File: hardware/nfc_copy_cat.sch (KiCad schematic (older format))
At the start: 35 parts, among them J1 USB_B_Micro, J2 Battery, J3 SWD, J4 NFC Module V3, J5 Conn_01x02, J6 Adafruit NFC 1.0, SW1 RST, SW2 Magspoof, SW3 NFC, U1 AP2112K-3.3TRG1, U2 MCP73831-2-OT, U3 TC4424, U4 ATSAMD21E18A, U5 GD25Q16C

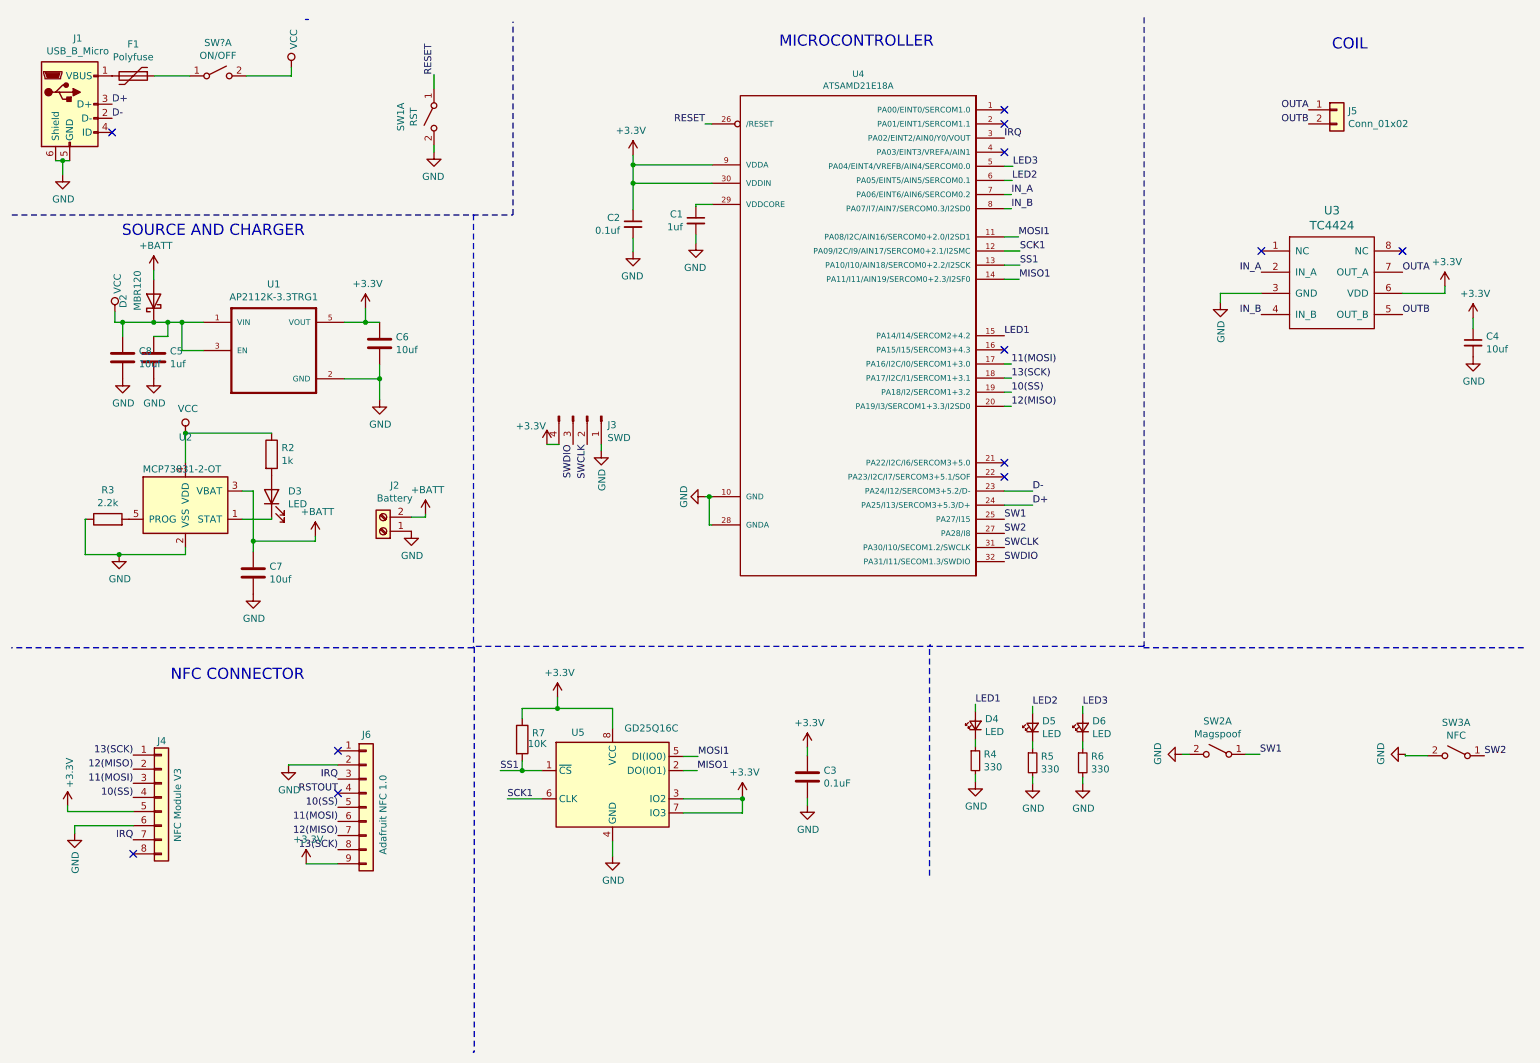
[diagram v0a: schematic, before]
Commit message: change battery source driver
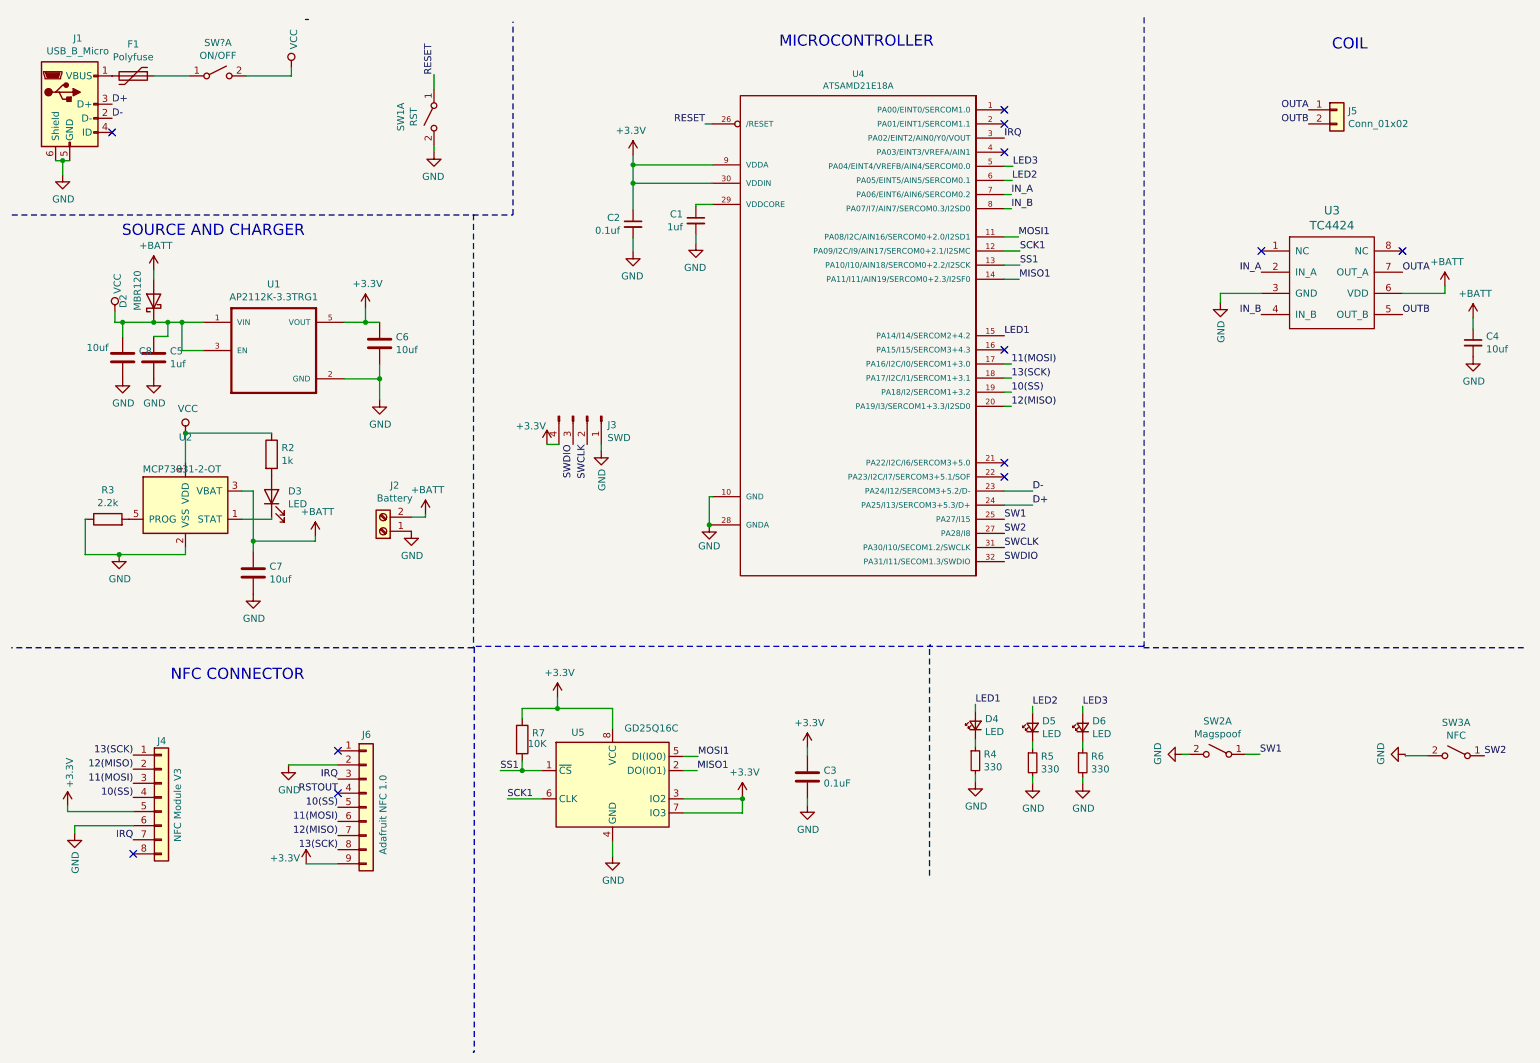
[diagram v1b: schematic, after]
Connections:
- net +3V3: no longer C4.1, U3.6 (VDD)
- net +BATT: now also C4.1, U3.6 (VDD)
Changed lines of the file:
@@
 L nfc_copy_cat-rescue:GND-MagSpoofTC-cache #PWR010
 U 1 1 5D10E10D
-P 5380 3860
-F 0 "#PWR010" H 5380 3610 50  0001 C CNN
-F 1 "GND" H 5380 3710 50  0000 C CNN
-F 2 "" H 5380 3860 50  0000 C CNN
-F 3 "" H 5380 3860 50  0000 C CNN
-	1    5380 3860
-	0    1    -1   0
-$EndComp
-Wire Wire Line
-	5380 3860 5410 3860
+P 5410 4060
+F 0 "#PWR010" H 5410 3810 50  0001 C CNN
+F 1 "GND" H 5410 3910 50  0000 C CNN
+F 2 "" H 5410 4060 50  0000 C CNN
+F 3 "" H 5410 4060 50  0000 C CNN
+	1    5410 4060
+	-1   0    0    -1
+$EndComp
 Text Label 5380 1220 2    50   ~ 0
 RESET
@@
 Wire Wire Line
 	5410 4060 5430 4060
-Connection ~ 5410 3860
 Wire Wire Line
 	5410 3860 5430 3860
@@
 P 1255 2875
 F 0 "C8" H 1370 2921 50  0000 L CNN
-F 1 "10uf" H 1370 2830 50  0000 L CNN
+F 1 "10uf" H 1000 2945 50  0000 L CNN
 F 2 "Capacitor_SMD:C_0805_2012Metric_Pad1.15x1.40mm_HandSolder" H 1293 2725 50  0001 C CNN
 F 3 "~" H 1255 2875 50  0001 C CNN
@@
 P 2555 6460
 F 0 "#PWR0101" H 2555 6310 50  0001 C CNN
-F 1 "+3.3V" H 2570 6633 50  0000 C CNN
+F 1 "+3.3V" H 2405 6500 50  0000 C CNN
 F 2 "" H 2555 6460 50  0001 C CNN
 F 3 "" H 2555 6460 50  0001 C CNN
@@
 	1700 3410 2310 3410
 NoConn ~ 2780 5960
-$Comp
-L power:+3.3V #PWR?
-U 1 1 5E3E4F66
-P 10820 2595
-F 0 "#PWR?" H 10820 2445 50  0001 C CNN
-F 1 "+3.3V" H 10835 2768 50  0000 C CNN
-F 2 "" H 10820 2595 50  0001 C CNN
-F 3 "" H 10820 2595 50  0001 C CNN
-	1    10820 2595
-	1    0    0    -1
-$EndComp
 Text Label 10320 2570 0    50   ~ 0
 OUTB
@@
 $EndComp
 $Comp
-L power:+3.3V #PWR019
-U 1 1 5D10F76C
-P 10620 2370
-F 0 "#PWR019" H 10620 2220 50  0001 C CNN
-F 1 "+3.3V" H 10635 2543 50  0000 C CNN
-F 2 "" H 10620 2370 50  0001 C CNN
-F 3 "" H 10620 2370 50  0001 C CNN
-	1    10620 2370
-	1    0    0    -1
-$EndComp
-$Comp
 L Device:C_Small C4
 U 1 1 5D11FCB0
@@
 	1255 2625 1200 2625
 Connection ~ 1700 3410
+Connection ~ 5410 4060
+$Comp
+L power:+BATT #PWR?
+U 1 1 6080D6FF
+P 10620 2370
+F 0 "#PWR?" H 10620 2220 50  0001 C CNN
+F 1 "+BATT" H 10635 2543 50  0000 C CNN
+F 2 "" H 10620 2370 50  0001 C CNN
+F 3 "" H 10620 2370 50  0001 C CNN
+	1    10620 2370
+	1    0    0    -1
+$EndComp
+$Comp
+L power:+BATT #PWR?
+U 1 1 6080F77B
+P 10820 2595
+F 0 "#PWR?" H 10820 2445 50  0001 C CNN
+F 1 "+BATT" H 10835 2768 50  0000 C CNN
+F 2 "" H 10820 2595 50  0001 C CNN
+F 3 "" H 10820 2595 50  0001 C CNN
+	1    10820 2595
+	1    0    0    -1
+$EndComp
 $EndSCHEMATC

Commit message: updateSchm
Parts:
- added C?: 1uf, Capacitor_SMD:C_0805_2012Metric_Pad1.15x1.40mm_HandSolder, symbol Device:C_Small
- added C?: 0.1uf, Capacitor_SMD:C_0805_2012Metric_Pad1.15x1.40mm_HandSolder, symbol Device:C_Small
- added U?: ATSAMD21E18A, Package_QFP:TQFP-32_7x7mm_P0.8mm, symbol nfc_copy_cat-rescue:ATSAMD21E18A-electroniccats
- U4: footprint Package_QFP:TQFP-32_7x7mm_P0.8mm -> Package_DFN_QFN:QFN-32-1EP_5x5mm_P0.5mm_EP3.6x3.6mm
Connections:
- net +3V3: now also C?.1, U?.30 (VDDIN), U?.9 (VDDA)
- net 10(SS): now also U?.19 (PA18/I2/SERCOM1+3.2)
- net 11(MOSI): now also U?.17 (PA16/I2C/I0/SERCOM1+3.0)
- net 12(MISO): now also U?.20 (PA19/I3/SERCOM1+3.3/I2SD0)
- net 13(SCK): now also U?.18 (PA17/I2C/I1/SERCOM1+3.1)
- net D+: now also U?.24 (PA25/I13/SERCOM3+5.3/D+)
- net D-: now also U?.23 (PA24/I12/SERCOM3+5.2/D-)
- net GND: now also C?.2, C?.2, U?.10 (GND), U?.28 (GNDA)
- net IN_A: now also U?.7 (PA06/EINT6/AIN6/SERCOM0.2)
- net IN_B: now also U?.8 (PA07/I7/AIN7/SERCOM0.3/I2SD0)
- net IRQ: now also U?.3 (PA02/EINT2/AIN0/Y0/VOUT)
- net LED1: now also U?.15 (PA14/I14/SERCOM2+4.2)
- net LED2: now also U?.6 (PA05/EINT5/AIN5/SERCOM0.1)
- net LED3: now also U?.5 (PA04/EINT4/VREFB/AIN4/SERCOM0.0)
- net MISO1: now also U?.14 (PA11/I11/AIN19/SERCOM0+2.3/I2SF0)
- net MOSI1: now also U?.11 (PA08/I2C/AIN16/SERCOM0+2.0/I2SD1)
- net RESET: now also U?.26 (/RESET)
- net SCK1: now also U?.12 (PA09/I2C/I9/AIN17/SERCOM0+2.1/I2SMC)
- net SS1: now also U?.13 (PA10/I10/AIN18/SERCOM0+2.2/I2SCK)
- net SW1: now also U?.25 (PA27/I15)
- net SW2: now also U?.27 (PA28/I8)
- net SWCLK: now also U?.31 (PA30/I10/SECOM1.2/SWCLK)
- net SWDIO: now also U?.32 (PA31/I11/SECOM1.3/SWDIO)
- new net: C?.1, U?.29 (VDDCORE)
- no-connect marks 12 -> 18
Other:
- note added: "BUTTONS"
- note added: "LEDS"
- note added: "QFN"
- note added: "SWD"
- note added: "TQFN"
- moved on the sheet: C1, C2, C3, C4, C5, C6, C7, C8, D2, D3, D4, D5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

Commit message: updatingPCB
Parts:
- removed C?: 1uf, Capacitor_SMD:C_0805_2012Metric_Pad1.15x1.40mm_HandSolder, symbol Device:C_Small
- removed C?: 0.1uf, Capacitor_SMD:C_0805_2012Metric_Pad1.15x1.40mm_HandSolder, symbol Device:C_Small
- gave numbers to parts that had none: 2
- renumbered C6 to C1, C8 to C3, C5 to C4, C1 to C5, C7 to C6, C3 to C7, C4 to C8, D2 to D1, D3 to D2, D4 to D3, D5 to D4, D6 to D5, J4 to J3, J6 to J4, J3 to J6, R2 to R1, R3 to R2, R7 to R3, SW1 to SW2, SW2 to SW3, SW3 to SW4, U4 to U2, U2 to U4, U3 to U5, U5 to U6
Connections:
- net VDDCORE: now reaches C5.1, U2.29 (VDDCORE)
- net VDDCORE: now also U3.29 (VDDCORE)
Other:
- moved on the sheet: C2, C5

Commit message: NRoutinginProgress
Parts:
- R1: footprint Resistor_SMD:R_0805_2012Metric_Pad1.15x1.40mm_HandSolder -> Resistor_SMD:R_0805_2012Metric
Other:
- moved on the sheet: F1
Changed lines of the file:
@@
 $EndDescr
-$Comp
-L nfc_copy_cat-rescue:USB_B_Micro-Connector J1
-U 1 1 5D106D67
-P 880 1080
-F 0 "J1" H 937 1547 50  0000 C CNN
-F 1 "USB_B_Micro" H 937 1456 50  0000 C CNN
-F 2 "Connectors:U254051N4BH806" H 1030 1030 50  0001 C CNN
-F 3 "~" H 1030 1030 50  0001 C CNN
-	1    880  1080
-	1    0    0    -1
-$EndComp
 $Comp
 L nfc_copy_cat-rescue:GND-MagSpoofTC-cache #PWR03
@@
 L Device:Polyfuse F1
 U 1 1 5D119569
-P 1330 880
-F 0 "F1" V 1105 880 50  0000 C CNN
-F 1 "Polyfuse" V 1196 880 50  0000 C CNN
-F 2 "Fuse:Fuse_0805_2012Metric_Pad1.15x1.40mm_HandSolder" H 1380 680 50  0001 L CNN
-F 3 "~" H 1330 880 50  0001 C CNN
-F 4 "MFU0805FF00500P100" V 1330 880 50  0001 C CNN "manf#"
-	1    1330 880
+P 1355 880
+F 0 "F1" V 1130 880 50  0000 C CNN
+F 1 "Polyfuse" V 1221 880 50  0000 C CNN
+F 2 "Fuse:Fuse_0805_2012Metric_Pad1.15x1.40mm_HandSolder" H 1405 680 50  0001 L CNN
+F 3 "~" H 1355 880 50  0001 C CNN
+F 4 "MFU0805FF00500P100" V 1355 880 50  0001 C CNN "manf#"
+	1    1355 880
 	0    1    1    0
 $EndComp
@@
 F 0 "R1" H 1960 3641 50  0000 L CNN
 F 1 "1k" H 1960 3550 50  0000 L CNN
-F 2 "Resistor_SMD:R_0805_2012Metric_Pad1.15x1.40mm_HandSolder" V 1820 3595 50  0001 C CNN
+F 2 "Resistor_SMD:R_0805_2012Metric" V 1820 3595 50  0001 C CNN
 F 3 "~" H 1890 3595 50  0001 C CNN
 	1    1890 3595
@@
 	1    0    0    -1
 $EndComp
-Wire Wire Line
-	1480 880  1730 880
 Wire Wire Line
 	2130 880  2450 880
@@
 Wire Wire Line
 	7940 1660 8045 1660
+$Comp
+L nfc_copy_cat-rescue:USB_B_Micro-Connector J1
+U 1 1 5D106D67
+P 880 1080
+F 0 "J1" H 937 1547 50  0000 C CNN
+F 1 "USB_B_Micro" H 937 1456 50  0000 C CNN
+F 2 "Connectors:U254051N4BH806" H 1030 1030 50  0001 C CNN
+F 3 "~" H 1030 1030 50  0001 C CNN
+	1    880  1080
+	1    0    0    -1
+$EndComp
+Wire Wire Line
+	1180 880  1205 880
+Wire Wire Line
+	1505 880  1730 880
 $EndSCHEMATC

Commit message: fixButtonSchm
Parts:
- removed SW2: RST, Button_Switch_SMD:SW_SPST_TL3342, symbol nfc_copy_cat-rescue:SW_DPST_x2-Switch
- removed SW3: Magspoof, Button_Switch_SMD:SW_SPST_TL3342, symbol nfc_copy_cat-rescue:SW_DPST_x2-Switch
- removed SW4: NFC, Button_Switch_SMD:SW_SPST_TL3342, symbol nfc_copy_cat-rescue:SW_DPST_x2-Switch
- added SW2: RST, Button_Switch_SMD:SW_SPST_TL3342, symbol Bast_WAN-cache:Switch_SW_Push
- added SW3: Magspoof, Button_Switch_SMD:SW_SPST_TL3342, symbol Bast_WAN-cache:Switch_SW_Push
- added SW4: NFC, Button_Switch_SMD:SW_SPST_TL3342, symbol Bast_WAN-cache:Switch_SW_Push
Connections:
- net GND: now also SW2.1, SW3.1, SW4.1
- net RESET: now also SW2.2
- net SW1: now also SW3.2
- net SW2: now also SW4.2
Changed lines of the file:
@@
 	-1   0    0    -1
 $EndComp
-Wire Wire Line
-	2955 1380 2955 1430
 $Comp
 L nfc_copy_cat-rescue:GND-MagSpoofTC-cache #PWR02
 U 1 1 5D116DE8
-P 2955 1430
-F 0 "#PWR02" H 2955 1180 50  0001 C CNN
-F 1 "GND" H 2960 1257 50  0000 C CNN
-F 2 "" H 2955 1430 50  0000 C CNN
-F 3 "" H 2955 1430 50  0000 C CNN
-	1    2955 1430
+P 600 7050
+F 0 "#PWR02" H 600 6800 50  0001 C CNN
+F 1 "GND" H 605 6877 50  0000 C CNN
+F 2 "" H 600 7050 50  0000 C CNN
+F 3 "" H 600 7050 50  0000 C CNN
+	1    600  7050
 	-1   0    0    -1
 $EndComp
-Wire Wire Line
-	2955 880  2955 980
-Text Label 2955 880  1    50   ~ 0
+Text Label 1150 7000 0    50   ~ 0
 RESET
-$Comp
-L nfc_copy_cat-rescue:SW_DPST_x2-Switch SW2
-U 1 1 5D1166AC
-P 2955 1180
-F 0 "SW2" H 2955 1415 50  0000 C CNN
-F 1 "RST" H 2955 1324 50  0000 C CNN
-F 2 "Button_Switch_SMD:SW_SPST_TL3342" H 2955 1180 50  0001 C CNN
-F 3 "~" H 2955 1180 50  0001 C CNN
-	1    2955 1180
-	0    -1   1    0
-$EndComp
 Wire Wire Line
 	4170 4010 4170 4210
@@
 Text Label 6260 4270 0    50   ~ 0
 SW2
-Wire Wire Line
-	965  7415 915  7415
 $Comp
 L nfc_copy_cat-rescue:GND-MagSpoofTC-cache #PWR039
 U 1 1 5D38B380
-P 915 7415
-F 0 "#PWR039" H 915 7165 50  0001 C CNN
-F 1 "GND" H 920 7242 50  0000 C CNN
-F 2 "" H 915 7415 50  0000 C CNN
-F 3 "" H 915 7415 50  0000 C CNN
-	1    915  7415
-	0    1    -1   0
-$EndComp
-Text Label 1465 7415 0    50   ~ 0
+P 1545 7080
+F 0 "#PWR039" H 1545 6830 50  0001 C CNN
+F 1 "GND" H 1550 6907 50  0000 C CNN
+F 2 "" H 1545 7080 50  0000 C CNN
+F 3 "" H 1545 7080 50  0000 C CNN
+	1    1545 7080
+	-1   0    0    -1
+$EndComp
+Text Label 2035 7000 0    50   ~ 0
 SW1
-$Comp
-L nfc_copy_cat-rescue:SW_DPST_x2-Switch SW3
-U 1 1 5D38B388
-P 1165 7415
-F 0 "SW3" H 1165 7650 50  0000 C CNN
-F 1 "Magspoof" H 1165 7559 50  0000 C CNN
-F 2 "Button_Switch_SMD:SW_SPST_TL3342" H 1165 7415 50  0001 C CNN
-F 3 "~" H 1165 7415 50  0001 C CNN
-	1    1165 7415
-	-1   0    0    -1
-$EndComp
-$Comp
-L nfc_copy_cat-rescue:SW_DPST_x2-Switch SW4
-U 1 1 5D3AF4BF
-P 2855 7425
-F 0 "SW4" H 2855 7660 50  0000 C CNN
-F 1 "NFC" H 2855 7569 50  0000 C CNN
-F 2 "Button_Switch_SMD:SW_SPST_TL3342" H 2855 7425 50  0001 C CNN
-F 3 "~" H 2855 7425 50  0001 C CNN
-	1    2855 7425
-	-1   0    0    -1
-$EndComp
 $Comp
 L nfc_copy_cat-rescue:GND-MagSpoofTC-cache #PWR040
 U 1 1 5D3B020B
-P 2495 7415
-F 0 "#PWR040" H 2495 7165 50  0001 C CNN
-F 1 "GND" H 2500 7242 50  0000 C CNN
-F 2 "" H 2495 7415 50  0000 C CNN
-F 3 "" H 2495 7415 50  0000 C CNN
-	1    2495 7415
-	0    1    -1   0
-$EndComp
-Wire Wire Line
-	2655 7425 2495 7425
-Wire Wire Line
-	2495 7425 2495 7415
-Text Label 3055 7425 0    50   ~ 0
+P 2430 7060
+F 0 "#PWR040" H 2430 6810 50  0001 C CNN
+F 1 "GND" H 2435 6887 50  0000 C CNN
+F 2 "" H 2430 7060 50  0000 C CNN
+F 3 "" H 2430 7060 50  0000 C CNN
+	1    2430 7060
+	-1   0    0    -1
+$EndComp
+Text Label 2920 7010 0    50   ~ 0
 SW2
 Text Label 6260 1470 0    50   ~ 0
 IRQ
-Wire Wire Line
-	1365 7415 1465 7415
 $Comp
 L Device:LED_Small D3
@@
 Wire Wire Line
 	7220 5830 7220 5895
-$Comp
-L nfc_copy_cat-rescue:SW_DPST_x2-Switch SW1
-U 1 1 607BCC65
-P 1930 880
-F 0 "SW1" H 1930 1115 50  0000 C CNN
-F 1 "ON/OFF" H 1930 1024 50  0000 C CNN
-F 2 "" H 1930 880 50  0001 C CNN
-F 3 "" H 1930 880 50  0001 C CNN
-	1    1930 880
-	1    0    0    -1
-$EndComp
 Wire Wire Line
 	2130 880  2450 880
@@
 Wire Notes Line
 	6965 6630 6965 6380
-Text Notes 1385 6760 0    79   ~ 0
+Text Notes 1100 6620 0    79   ~ 0
 BUTTONS
 Wire Notes Line
@@
 Wire Wire Line
 	1505 880  1730 880
+$Comp
+L nfc_copy_cat-rescue:SW_DPST_x2-Switch SW1
+U 1 1 607BCC65
+P 1930 880
+F 0 "SW1" H 1930 1115 50  0000 C CNN
+F 1 "ON/OFF" H 1930 1024 50  0000 C CNN
+F 2 "" H 1930 880 50  0001 C CNN
+F 3 "" H 1930 880 50  0001 C CNN
+	1    1930 880
+	1    0    0    -1
+$EndComp
+$Comp
+L Bast_WAN-cache:Switch_SW_Push SW2
+U 1 1 610BBDBF
+P 910 7000
+F 0 "SW2" H 1010 7250 50  0000 R CNN
+F 1 "RST" H 1000 7175 50  0000 R CNN
+F 2 "Button_Switch_SMD:SW_SPST_TL3342" H 910 7200 50  0001 C CNN
+F 3 "" H 910 7200 50  0001 C CNN
+	1    910  7000
+	1    0    0    -1
+$EndComp
+Wire Wire Line
+	1150 7000 1110 7000
+Wire Wire Line
+	600  7050 600  7000
+Wire Wire Line
+	600  7000 710  7000
+$Comp
+L Bast_WAN-cache:Switch_SW_Push SW3
+U 1 1 61103185
+P 1780 7000
+F 0 "SW3" H 1880 7250 50  0000 R CNN
+F 1 "Magspoof" H 1950 7180 50  0000 R CNN
+F 2 "Button_Switch_SMD:SW_SPST_TL3342" H 1780 7200 50  0001 C CNN
+F 3 "" H 1780 7200 50  0001 C CNN
+	1    1780 7000
+	1    0    0    -1
+$EndComp
+Wire Wire Line
+	1545 7080 1545 7000
+Wire Wire Line
+	1545 7000 1580 7000
+Wire Wire Line
+	2035 7000 1980 7000
+$Comp
+L Bast_WAN-cache:Switch_SW_Push SW4
+U 1 1 61120039
+P 2670 7010
+F 0 "SW4" H 2770 7260 50  0000 R CNN
+F 1 "NFC" H 2755 7185 50  0000 R CNN
+F 2 "Button_Switch_SMD:SW_SPST_TL3342" H 2670 7210 50  0001 C CNN
+F 3 "" H 2670 7210 50  0001 C CNN
+	1    2670 7010
+	1    0    0    -1
+$EndComp
+Wire Wire Line
+	2430 7060 2430 7010
+Wire Wire Line
+	2430 7010 2470 7010
+Wire Wire Line
+	2870 7010 2920 7010
 $EndSCHEMATC

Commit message: addSwitch
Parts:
- added D3: LED, LED_SMD:LED_0805_2012Metric_Pad1.15x1.40mm_HandSolder, symbol Device:LED_Small
- added R4: 330, Resistor_SMD:R_0805_2012Metric, symbol Device:R_Small
- SW1: footprint (none) -> hardware:Micro_interruptor_SPDT
- renumbered D3 to D4, D4 to D5, D5 to D6, R4 to R5, R5 to R6, R6 to R7
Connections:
- net GND: now also R4.2
- net VCC: now also D3.2 (A)
- new net: D3.1 (K), R4.1
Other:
- moved on the sheet: D4, D5, D6, R5, R6, R7

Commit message: update v1.6
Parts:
- SW2, SW3, SW4: symbol Bast_WAN-cache:Switch_SW_Push -> nfc_copy_cat-rescue:Switch_SW_Push-Bast_WAN-cache
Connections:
- net VCC: now also F1.1; no longer C3.1, U1.1 (VIN), U1.3 (EN)
- net at SW1.1 (A): now also C3.1, U1.1 (VIN), U1.3 (EN); no longer F1.1
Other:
- moved on the sheet: C1, C3, C4, D1, F1, SW1A, U1
